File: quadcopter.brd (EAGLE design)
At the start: 57.1 x 53.3 mm, 66 parts, among them J1 ISP, J3 POWER_JACKPTH_LOCK, M1 MOTOR_PADS, M2 MOTOR_PADS, M3 MOTOR_PADS, M4 MOTOR_PADS, U1 ATMEGA128RFA1, U2 LM1117, Y1 16MHz, Y2 32.768kHz

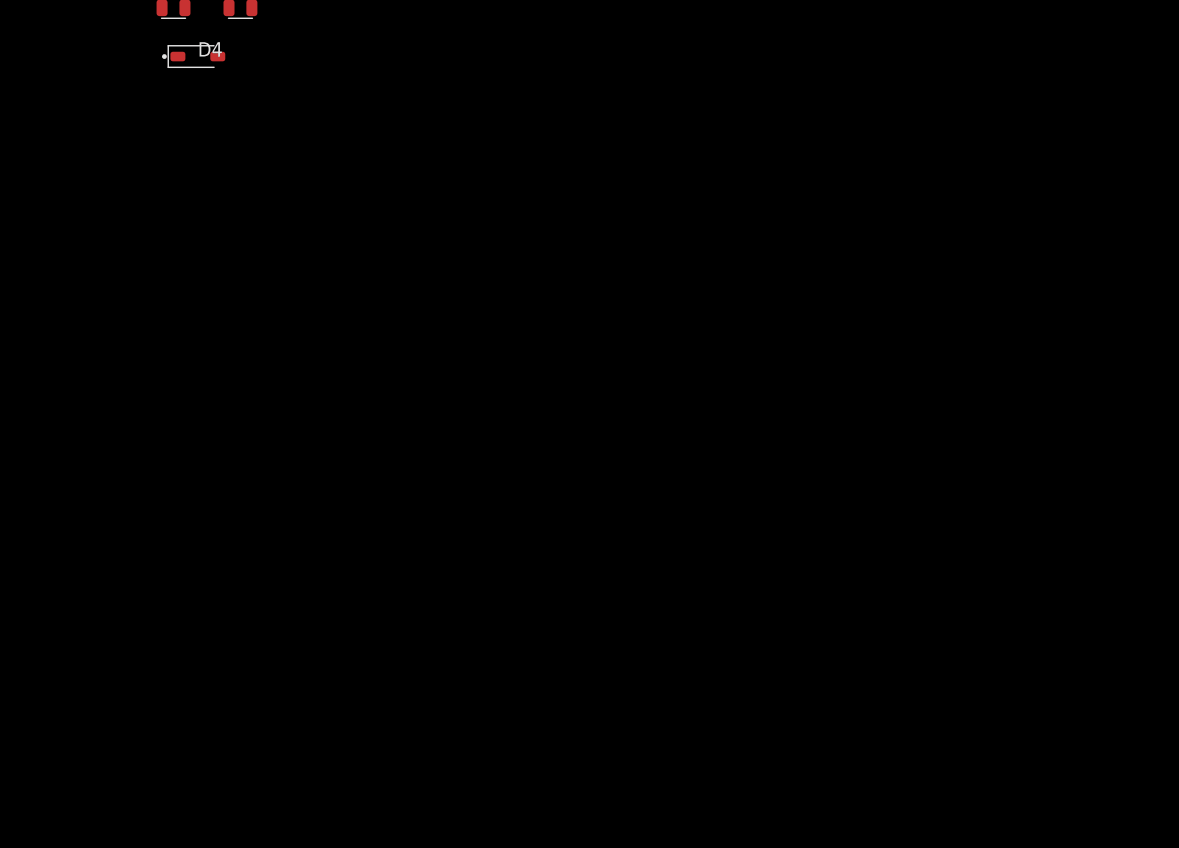
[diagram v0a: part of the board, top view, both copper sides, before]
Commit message: voltage reg added
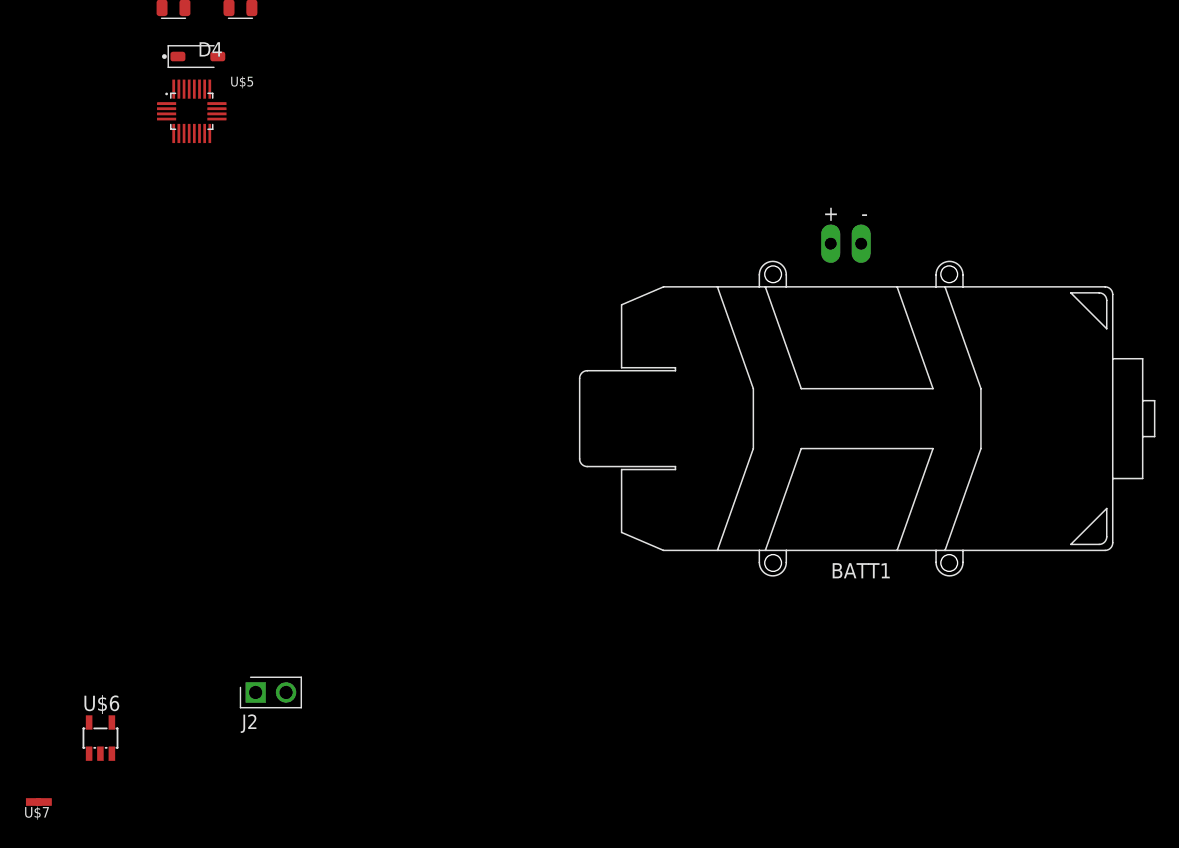
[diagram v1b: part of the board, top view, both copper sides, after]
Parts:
- added BATT1: BATTERY-HUBSAN-W/HOLDER, quadparts_prebuilt:BATTERY-W/HOLDER-380MAH-HUBSAN
- added J2: (no value), quadparts_jay:MALE_HEADER_2X1_0.1IN
- added U$5: IMU_497-14946-1-ND, quadparts_jay:IMU_497-14946-1-ND
- added U$6: TPS73633-DBVT, quadparts_prebuilt:SOT23-DBV
- added U$7: NET_BRIDGE, quadparts_jay:NET_BRIDGE
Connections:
- new net BAT_GND: U$7.P$2
- new net N$11: J2.1
- new net N$12: J2.2
- new net N$14: U$6.1
- new net N$15: U$6.2
- new net N$16: U$6.3
- new net N$17: U$6.5
- new net N$18: U$6.4
- new net VBAT: BATT1.+
- net GND: now also BATT1.-, U$7.P$1
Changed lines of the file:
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@@
 <?xml version="1.0" encoding="utf-8"?>
 <!DOCTYPE eagle SYSTEM "eagle.dtd">
-<eagle version="8.1.1">
+<eagle version="8.1.0">
 <drawing>
 <settings>
@@
 <attribute name="REVIEWER" value="" x="-29.464" y="-126.746" size="1.778" layer="27" display="off"/>
 </element>
+<element name="U$5" library="quadparts_jay" package="IMU_497-14946-1-ND" value="IMU_497-14946-1-ND" x="-13.208" y="-133.604">
+<attribute name="CREATOR" value="Jay Ives" x="-13.208" y="-133.604" size="1.778" layer="27" display="off"/>
+<attribute name="DIST" value="Digikey" x="-13.208" y="-133.604" size="1.778" layer="27" display="off"/>
+<attribute name="DISTPN" value="497-14946-1-ND" x="-13.208" y="-133.604" size="1.778" layer="27" display="off"/>
+<attribute name="MFR" value="STMicroelectronics" x="-13.208" y="-133.604" size="1.778" layer="27" display="off"/>
+<attribute name="MPN" value="LSM9DS1TR" x="-13.208" y="-133.604" size="1.778" layer="27" display="off"/>
+<attribute name="REVIEWER" value="" x="-13.208" y="-133.604" size="1.778" layer="27" display="off"/>
+</element>
+<element name="BATT1" library="quadparts_prebuilt" package="BATTERY-W/HOLDER-380MAH-HUBSAN" value="BATTERY-HUBSAN-W/HOLDER" x="42.672" y="-159.258">
+<attribute name="CREATOR" value="Swanson" x="42.672" y="-159.258" size="1.778" layer="27" display="off"/>
+<attribute name="DIST" value="AMAZON" x="42.672" y="-159.258" size="1.778" layer="27" display="off"/>
+<attribute name="DISTPN" value="http://www.amazon.com/dp/B00RROB6Q4?smid=AMNTPWSAB5H0S" x="42.672" y="-159.258" size="1.778" layer="27" display="off"/>
+<attribute name="MFR" value="HUBSAN" x="42.672" y="-159.258" size="1.778" layer="27" display="off"/>
+<attribute name="MPN" value="X4-H107C-8-in-1" x="42.672" y="-159.258" size="1.778" layer="27" display="off"/>
+</element>
+<element name="J2" library="quadparts_jay" package="MALE_HEADER_2X1_0.1IN" value="" x="-7.874" y="-182.118">
+<attribute name="CREATOR" value="SWANSON" x="-7.874" y="-182.118" size="1.778" layer="27" display="off"/>
+<attribute name="DIST" value="Digikey" x="-7.874" y="-182.118" size="1.778" layer="27" display="off"/>
+<attribute name="DISTPN" value="3M9447-ND" x="-7.874" y="-182.118" size="1.778" layer="27" display="off"/>
+<attribute name="MFR" value="3M" x="-7.874" y="-182.118" size="1.778" layer="27" display="off"/>
+<attribute name="MPN" value="961102-6404-AR" x="-7.874" y="-182.118" size="1.778" layer="27" display="off"/>
+<attribute name="REVIEWER" value="" x="-7.874" y="-182.118" size="1.778" layer="27" display="off"/>
+</element>
+<element name="U$6" library="quadparts_prebuilt" package="SOT23-DBV" value="TPS73633-DBVT" x="-20.828" y="-185.928">
+<attribute name="DATASHEET" value="http://www.ti.com/lit/ds/symlink/lp3985.pdf" x="-20.828" y="-185.928" size="1.778" layer="27" display="off"/>
+<attribute name="DIST" value="Digikey" x="-20.828" y="-185.928" size="1.778" layer="27" display="off"/>
+<attribute name="DISTPN" value="LP3985IM5X-3.0/NOPBCT-ND" x="-20.828" y="-185.928" size="1.778" layer="27" display="off"/>
+<attribute name="MFR" value="Texas Instruments" x="-20.828" y="-185.928" size="1.778" layer="27" display="off"/>
+<attribute name="MPN" value="LP3985IM5X-3.0/NOPB" x="-20.828" y="-185.928" size="1.778" layer="27" display="off"/>
+<attribute name="PRICE" value="0.59" x="-20.828" y="-185.928" size="1.778" layer="27" display="off"/>
+</element>
+<element name="U$7" library="quadparts_jay" package="NET_BRIDGE" value="NET_BRIDGE" x="-26.416" y="-191.262">
+<attribute name="CREATOR" value="Chris Miranda" x="-26.416" y="-191.262" size="1.778" layer="27" display="off"/>
+<attribute name="DIST" value="none" x="-26.416" y="-191.262" size="1.778" layer="27" display="off"/>
+<attribute name="DISTPN" value="none" x="-26.416" y="-191.262" size="1.778" layer="27" display="off"/>
+<attribute name="MFR" value="none" x="-26.416" y="-191.262" size="1.778" layer="27" display="off"/>
+<attribute name="MPN" value="none" x="-26.416" y="-191.262" size="1.778" layer="27" display="off"/>
+<attribute name="REVIEWER" value="" x="-26.416" y="-191.262" size="1.778" layer="27" display="off"/>
+</element>
 </elements>
 <signals>
@@
 <contactref element="C22" pad="2"/>
 <contactref element="U$4" pad="P$2"/>
+<contactref element="BATT1" pad="-"/>
+<contactref element="U$7" pad="P$1"/>
+<wire x1="-10.099" y1="-124.968" x2="-26.416" y2="-191.262" width="0" layer="19" extent="1-1"/>
 <wire x1="-7.233" y1="-117.348" x2="-10.099" y2="-124.968" width="0" layer="19" extent="1-1"/>
 <wire x1="-13.6995" y1="-111.97" x2="-7.233" y2="-117.348" width="0" layer="19" extent="1-1"/>
@@
 <wire x1="7.62" y1="33.02" x2="12.05" y2="31.75" width="0" layer="19" extent="1-1"/>
 <wire x1="11.176" y1="47.625" x2="7.62" y2="33.02" width="0" layer="19" extent="1-1"/>
+<wire x1="42.672" y1="-144.653" x2="-10.099" y2="-124.968" width="0" layer="19" extent="1-1"/>
 </signal>
 <signal name="N$3">
@@
 <wire x1="-14.732" y1="-34.588" x2="-11.462" y2="-45.212" width="0" layer="19" extent="1-1"/>
 </signal>
+<signal name="VBAT">
+<contactref element="BATT1" pad="+"/>
+</signal>
+<signal name="N$11">
+<contactref element="J2" pad="1"/>
+</signal>
+<signal name="N$12">
+<contactref element="J2" pad="2"/>
+</signal>
+<signal name="N$14">
+<contactref element="U$6" pad="1"/>
+</signal>
+<signal name="N$15">
+<contactref element="U$6" pad="2"/>
+</signal>
+<signal name="N$16">
+<contactref element="U$6" pad="3"/>
+</signal>
+<signal name="N$17">
+<contactref element="U$6" pad="5"/>
+</signal>
+<signal name="N$18">
+<contactref element="U$6" pad="4"/>
+</signal>
+<signal name="BAT_GND">
+<contactref element="U$7" pad="P$2"/>
+</signal>
 </signals>

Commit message: Added all parts to board but have yet to run autorouter/set up the traces
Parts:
- removed B1: 748421245, SparkFun-RF:BALUN
- removed C10, C14: 10uF, SparkFun-Passives:EIA3216
- removed C11: 22pF, SparkFun-Passives:0402-CAP
- removed C12: 1uF, SparkFun-Passives:0402-CAP
- removed C13: 0.1uF, SparkFun-Passives:0402-CAP
- removed C9: 0.75pF, SparkFun-Passives:0402-CAP
- removed J1: ISP, SparkFun-Connectors:2X3-NS
- removed J2: (no value), quadparts_jay:MALE_HEADER_2X1_0.1IN
- removed J3: POWER_JACKPTH_LOCK, SparkFun-Connectors:POWER_JACK_PTH_LOCK
- removed JP1, JP9: FTDI, SparkFun-Connectors:FTDI_BASIC
- removed JP6: (no value), SparkFun-Connectors:JST-2-PTH
- removed JP7: (no value), SparkFun-Connectors:1X02_NO_SILK
- removed JP8: (no value), SparkFun-Connectors:SCREWTERMINAL-3.5MM-2-NS
- removed LED1: RED, SparkFun-LED:LED-0603
- removed LED2, LED3: GREEN, SparkFun-LED:LED-0603
- removed S2: (no value), SparkFun:SWITCH-SPST-SMD-A
- removed U$6: TPS73633-DBVT, quadparts_prebuilt:SOT23-DBV
- removed U$7: NET_BRIDGE, quadparts_jay:NET_BRIDGE
- removed U2: LM1117, SparkFun:SOT223
- removed Y2: 32.768kHz, SparkFun-FreqCtrl:CRYSTAL-32KHZ-SMD
- added B2: BALUN0805, quadparts_prebuilt:BALUN
- added C24, C25: 1uF, quadparts_prebuilt:CAPC2012X140_HS
- added C26, C30: 0.01uF, quadparts_prebuilt:CAPC2012X140_HS
- added C27, C28, C29: 0.1uF, quadparts_prebuilt:CAPC2012X140_HS
- added C31: 10uF, quadparts_prebuilt:CAPC2012X140_HS
- added D5, D6: green, quadparts_prebuilt:LEDSC125X200X120-2_HS
- added DEBUGGING_HEADER: (no value), quadparts_prebuilt:HDRV10W63P254_10X1_2540X254H838_HS
- added FRONT_LED_1, FRONT_LED_2: GREEN, LEDs:KINGBRIGHT_LED
- added J4: AVR_SPI_PRG_6NS, quadparts_prebuilt:2X3-NS
- added JP2, JP3: FTDI_BASICPTH, quadparts_prebuilt:FTDI_BASIC
- added NET_BRIDGE: NET_BRIDGE, quadparts_jay:NET_BRIDGE
- added POWER_SWITCH: (no value), quadparts_jay:MALE_HEADER_2X1_0.1IN
- added R15: 20, quadparts_prebuilt:RESC2012X60_HS
- added VOLTAGE_REGULATOR: TPS73633-DBVT, quadparts_prebuilt:SOT23-DBV
- C1, C2: device SparkFun-Passives:0402-CAP -> quadparts_prebuilt:CAPC2012X140_HS
- C3, C4: value 1uF -> 12pF; device SparkFun-Passives:0402-CAP -> quadparts_prebuilt:CAPC2012X140_HS
- C5: value 12pF -> 0.75pF; device SparkFun-Passives:0402-CAP -> quadparts_prebuilt:CAPC2012X140_HS
- C6: value 12pF -> 22pF; device SparkFun-Passives:0402-CAP -> quadparts_prebuilt:CAPC2012X140_HS
- C7, C8: value 12pF -> 1uF; device SparkFun-Passives:0402-CAP -> quadparts_prebuilt:CAPC2012X140_HS
- R1: value 10k -> 10K; device SparkFun-Passives:0402-RES -> quadparts_prebuilt:RESC2012X60_HS
- R2: value 1k -> 10K; device SparkFun-Passives:0402-RES -> quadparts_prebuilt:RESC2012X60_HS
- R3: value 240 -> 10K; device SparkFun:0402-RES -> quadparts_prebuilt:RESC2012X60_HS
- R4: value 390 -> 20; device SparkFun:0402-RES -> quadparts_prebuilt:RESC2012X60_HS
- R5, R6: device SparkFun:0402-RES -> quadparts_prebuilt:RESC2012X60_HS
- Y1: value 16MHz -> (none); device SparkFun-FreqCtrl:CRYSTAL-SMD-5X3 -> quadparts_prebuilt:CRYSTAL-SMD-5X3
- moved BATT1 166.8 mm to (-2.54, 1.27), flipped to the bottom
- moved U$5 134.3 mm to (0.00, 0.00)
- moved D4 131.4 mm to (-48.3, -2.54)
- moved R13 129.9 mm to (-39.4, 2.54), turned to 180 degrees
- moved D2 129.8 mm to (-1.27, 49.5), turned to 270 degrees
- moved M2 127.9 mm to (1.27, 57.1)
- moved R14 127.1 mm to (-43.2, -2.54), turned to 90 degrees
- moved M4 124.8 mm to (-54.6, -1.27), turned to 90 degrees
- moved R9 121.0 mm to (0.00, 44.5)
- moved R10 119.7 mm to (5.08, 43.2), turned to 270 degrees
- moved C22 119.3 mm to (-40.6, -2.54), turned to 270 degrees
- moved U$4 117.3 mm to (-47.0, 2.54), turned to 90 degrees
- moved C23 112.9 mm to (-31.8, 0.00), turned to 90 degrees
- moved U$2 112.0 mm to (3.81, 49.5)
- moved C18 110.3 mm to (0.00, 41.9)
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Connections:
- removed net 3V: C10.A, C12.1, C3.1, C4.1, R1.2, R2.2, R3.2, U1.23, U1.34, U1.44, U1.54, U1.59, U2.2
- removed net FB: R3.1, R4.2, U2.1
- removed net FILTERED: R10.2, R11.2, R12.2, R13.2, R14.2, R7.2, R8.2, R9.2
- removed net FLYBACK: D1.A, D2.A, D3.A, D4.A, M1.V-, M2.V-, M3.V-, M4.V-, U$1.P$3, U$2.P$3, U$3.P$3, U$4.P$3
- removed net N$11: J2.1
- removed net N$12: J2.2
- removed net N$14: U$6.1
- removed net N$15: U$6.2
- removed net N$16: U$6.3
- removed net N$17: U$6.5
- removed net N$6: C8.1, U1.17, Y2.X2
- removed net N$9: J3.PWR, JP6.2, JP7.2, JP8.2, S2.2
- removed net VCC: C13.1, C14.A, C17.1, C19.1, C21.1, C23.1, D1.C, D2.C, D3.C, D4.C, M1.V+, M2.V+, M3.V+, M4.V+, S2.1, U2.3
- new net 3.0V: C25.1, C27.1, C28.1, C31.1, C7.1, C8.1, DEBUGGING_HEADER.7, R1.2, R2.2, R3.1, U$5.P$1, U$5.P$22, U$5.P$23, U$5.P$3, U$5.P$5, U$5.P$7, U$5.P$8, U1.23, U1.34, U1.44, U1.54, U1.59, VOLTAGE_REGULATOR.5
- new net FILTERED1: R13.2, R14.2, U$4.P$1
- new net FILTERED2: R10.2, R9.2, U$2.P$1
- new net FILTERED3: R11.2, R12.2, U$3.P$1
- new net FILTERED4: R7.2, R8.2, U$1.P$1
- new net FLYBACK1: D4.A, M4.V-, U$4.P$3
- new net FLYBACK2: D2.A, M2.V-, U$2.P$3
- new net FLYBACK3: D3.A, M3.V-, U$3.P$3
- new net FLYBACK4: D1.A, M1.V-, U$1.P$3
- new net N$1: FRONT_LED_1.P$2, R4.1
- new net N$10: C29.1, U$5.P$24
- new net V: BATT1.+, POWER_SWITCH.2
- net AVDD: now also C2.1; no longer C1.1
- net BAT_GND: now also BATT1.-, C16.2, C17.2, C18.2, C19.2, C20.2, C21.2, C22.2, C23.2, DEBUGGING_HEADER.9, NET_BRIDGE.P$2, R10.1, R12.1, R14.1, R8.1, U$1.P$2, U$2.P$2, U$3.P$2, U$4.P$2; no longer U$7.P$2
- net DTR: now also JP2.DTR; no longer JP9.DTR
- net DVDD: now also C1.1; no longer C2.1
- net GND: now also B2.1, C24.1, C25.2, C26.2, C27.2, C28.2, C29.2, C30.2, C31.2, C6.1, D5.C, D6.C, DEBUGGING_HEADER.10, J4.6, JP2.GND, JP3.GND, NET_BRIDGE.P$1, R15.2, R4.2, U$5.P$14, U$5.P$15, U$5.P$16, U$5.P$17, U$5.P$18, U$5.P$19, U$5.P$20, U$5.P$6, VOLTAGE_REGULATOR.2; no longer B1.5, BATT1.-, C10.C, C11.2, C12.2, C13.2, C14.C, C16.2, C17.2, C18.2, C19.2, C20.2, C21.2, C22.2, C23.2, C6.2, C9.1, J1.6, J3.GND, J3.GNDBREAK, JP6.1, JP7.1, JP8.1, JP9.GND, LED1.C, LED2.C, LED3.C, R10.1, R12.1, R14.1, R4.1, R8.1, U$1.P$2, U$2.P$2, U$3.P$2, U$4.P$2, U$7.P$1
- net MISO: now also J4.1; no longer J1.1
- net MOSI: now also J4.4; no longer J1.4
- net N$13: now also D6.A; no longer LED2.A
- net N$18: now also C26.1, VOLTAGE_REGULATOR.4; no longer U$6.4
- net N$2: now also C30.1, U$5.P$21; no longer LED1.A, R2.1
- net N$3: now also C4.1; no longer C5.1
- net N$4: now also C3.1; no longer C6.1
- net N$5: now also FRONT_LED_2.P$2, R15.1; no longer C7.1, U1.18, Y2.X1
- net N$7: now also B2.2, C6.2; no longer B1.2, C11.1
- net N$8: now also D5.A; no longer LED3.A
- net PB5: now also DEBUGGING_HEADER.6
- net PE3: now also DEBUGGING_HEADER.4
- net PE4: now also DEBUGGING_HEADER.3
- net PE5: now also DEBUGGING_HEADER.5
- net RESET: now also J4.5; no longer J1.5
- net RFANT: now also B2.5, C5.1; no longer B1.1, C9.2
- net RFN: now also B2.4; no longer B1.3
- net RFP: now also B2.3; no longer B1.4
- net RX0: now also JP2.TXO; no longer JP9.TXO
- net RX1: now also JP3.RXI
- net SCK: now also J4.3; no longer J1.3
- net SCL: now also DEBUGGING_HEADER.1, R2.1, U$5.P$2
- net SDA: now also DEBUGGING_HEADER.2, R3.2, U$5.P$4
- net TX0: now also JP2.RXI; no longer JP9.RXI
- net TX1: now also JP3.TXO
- net VBAT: now also C17.1, C19.1, C21.1, C23.1, C24.2, D1.C, D2.C, D3.C, D4.C, DEBUGGING_HEADER.8, FRONT_LED_1.P$1, FRONT_LED_2.P$1, M1.V+, M2.V+, M3.V+, M4.V+, POWER_SWITCH.1, VOLTAGE_REGULATOR.1, VOLTAGE_REGULATOR.3; no longer BATT1.+
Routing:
- net 3V: track 141.7 -> 0.00 mm, vias 7 -> 0
- net RESET: track 121.3 -> 0.00 mm, vias 2 -> 0
- net RX0: track 101.3 -> 0.00 mm, vias 2 -> 0
- net GND: track 98.6 -> 0.00 mm, vias 36 -> 0
- net TX0: track 92.4 -> 0.00 mm, vias 2 -> 0
- net MOSI: track 88.1 -> 0.00 mm
- net MISO: track 85.7 -> 0.00 mm
- net SCK: track 82.6 -> 0.00 mm, vias 1 -> 0
- net AREF: track 80.3 -> 0.00 mm
- net PE3: track 60.3 -> 0.00 mm, vias 2 -> 0
- net PB5: track 59.0 -> 0.00 mm
- net PE4: track 55.5 -> 0.00 mm, vias 2 -> 0
- net VCC: track 55.2 -> 0.00 mm, vias 2 -> 0
- net PB4: track 54.0 -> 0.00 mm
- net PE5: track 52.7 -> 0.00 mm, vias 2 -> 0
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- removed copper zone on layer 1, net GND
- removed copper zone on layer 16, net GND
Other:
- board size 57.1 x 53.3 mm -> 137.2 x 137.2 mm
- board text removed: "0"
- board text removed: "1"
- board text removed: "2"
- board text removed: "3"
- board text removed: "3.3V"
- board text removed: "4"
- board text removed: "4.5-15V"
- board text removed: "5"
- board text removed: "6"
- board text removed: "7"
- board text removed: "ANALOG (PORT F)"
- board text removed: "AREF"
- board text removed: "ATmega128RFA1"
- board text removed: "B0"
- board text removed: "B1"
- board text removed: "B2"
- board text removed: "B3"
- board text removed: "B4"
- board text removed: "B5"
- board text removed: "B6"
- board text removed: "B7"
- board text removed: "CLKI"
- board text removed: "D0"
- board text removed: "D1"
- board text removed: "D2"
- board text removed: "D3"
- board text removed: "D4"
- board text removed: "D5"
- board text removed: "D6"
- board text removed: "D7"
- board text removed: "DTR"
- board text removed: "Dev Board"
- board text removed: "E0"
- board text removed: "E1"
- board text removed: "E2"
- board text removed: "E3"
- board text removed: "E4"
- board text removed: "E5"
- board text removed: "E6"
- board text removed: "E7"
- board text removed: "G0"
- board text removed: "G1"
- board text removed: "G2"
- board text removed: "G5"
- board text removed: "GND"
- board text removed: "MISO"
- board text removed: "MOSI"
- board text removed: "OFF"
- board text removed: "ON"
- board text removed: "PWR"
- board text removed: "RST"
- board text removed: "RX0"
- board text removed: "RX1"
- board text removed: "Reset"
- board text removed: "SCK"
- board text removed: "SCL"
- board text removed: "SDA"
- board text removed: "SSN"
- board text removed: "TST"
- board text removed: "TX0"
- board text removed: "TX1"
- board text removed: "VIN"
- board text removed: "v23"

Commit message: Fixed some schematic things, still need to fix swanson notes and the motor drivers
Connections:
- net 3.0V: now also U$5.P$13
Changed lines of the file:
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@@
 <contactref element="R3" pad="1"/>
 <contactref element="R2" pad="2"/>
+<contactref element="U$5" pad="P$13"/>
 <wire x1="-13.45" y1="-33.71" x2="-16.825" y2="-35.56" width="0" layer="19" extent="1-1"/>
 <wire x1="-8.2" y1="-32.46" x2="-13.45" y2="-33.71" width="0" layer="19" extent="1-1"/>
@@
 <wire x1="7.245" y1="-21.59" x2="-8.2" y2="-27.46" width="0" layer="19" extent="1-1"/>
 <wire x1="5.455" y1="-17.78" x2="7.245" y2="-21.59" width="0" layer="19" extent="1-1"/>
-<wire x1="-0.645" y1="-1.85" x2="5.455" y2="-17.78" width="0" layer="19" extent="1-1"/>
+<wire x1="1.505" y1="-1.85" x2="5.455" y2="-17.78" width="0" layer="19" extent="1-1"/>
+<wire x1="-0.645" y1="-1.85" x2="1.505" y2="-1.85" width="0" layer="19" extent="1-1"/>
 <wire x1="-1.075" y1="-1.85" x2="-0.645" y2="-1.85" width="0" layer="19" extent="1-1"/>
 <wire x1="-2.1" y1="-0.645" x2="-1.075" y2="-1.85" width="0" layer="19" extent="1-1"/>

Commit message: Modify Motor Driver and check off components on swanson_design_review
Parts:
- removed C16, C18, C20, C22: 1uF, quadparts_prebuilt:CAPC2012X140_HS
- added C10, C11, C12, C9: 0.1uF, quadparts_prebuilt:CAPC2012X140_HS
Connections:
- net BAT_GND: now also C10.2, C11.2, C12.2, C9.2; no longer C16.2, C18.2, C20.2, C22.2
- net PB5: now also C9.1; no longer C22.1
- net PE3: now also C10.1; no longer C20.1
- net PE4: now also C11.1; no longer C16.1
- net PE5: now also C12.1; no longer C18.1
